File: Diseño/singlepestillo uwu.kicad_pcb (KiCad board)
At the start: 2 copper layers, 17 parts, among them J1 MAX98357A, J2 Conn_01x03_Pin, J3 Screw_Terminal_01x03, J5 Screw_Terminal_01x02, J9 Screw_Terminal_01x03, K3 G6AU, Q6 MMBT2222A, U3 EL817, U5 L7805, U6 ESP32DevKitv1

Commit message: avance pcb
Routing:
- net RV-VCC: track 151.4 -> 150.8 mm
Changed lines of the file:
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@@
-	)
-	(segment
-		(start 161.2 52.8)
-		(end 158.8 52.8)
-		(width 1)
-		(layer "B.Cu")
-		(net 3)
-	)
-	(segment
-		(start 158.8 52.8)
-		(end 153.4 47.4)
-		(width 1)
-		(layer "B.Cu")
-		(net 3)
 	)
 	(segment
@@
 	)
 	(segment
+		(start 161.758131 55.749)
+		(end 161.058131 55.049)
+		(width 1)
+		(layer "B.Cu")
+		(net 3)
+	)
+	(segment
 		(start 141.4 47.8)
 		(end 140.4 48.8)
@@
 	)
 	(segment
-		(start 163.891869 55.049)
-		(end 163.449 55.049)
+		(start 151.126 45.799)
+		(end 150.399 45.799)
 		(width 1)
 		(layer "B.Cu")
@@
 	)
 	(segment
-		(start 151.126 45.799)
-		(end 150.399 45.799)
+		(start 153.4 47.4)
+		(end 152.065 47.4)
+		(width 1)
+		(layer "B.Cu")
+		(net 3)
+	)
+	(segment
+		(start 163.449 55.749)
+		(end 161.758131 55.749)
+		(width 1)
+		(layer "B.Cu")
+		(net 3)
+	)
+	(segment
+		(start 161.049 55.049)
+		(end 153.4 47.4)
 		(width 1)
 		(layer "B.Cu")
@@
 	)
 	(segment
-		(start 165.7 58)
-		(end 163.891869 56.191869)
+		(start 133.069706 35.2)
+		(end 135.334853 37.465147)
 		(width 1)
 		(layer "B.Cu")
@@
 	)
 	(segment
-		(start 133.069706 35.2)
-		(end 135.334853 37.465147)
+		(start 161.058131 55.049)
+		(end 161.049 55.049)
 		(width 1)
 		(layer "B.Cu")
@@
 	)
 	(segment
-		(start 163.891869 56.191869)
-		(end 163.891869 55.049)
+		(start 165.7 58)
+		(end 163.449 55.749)
 		(width 1)
 		(layer "B.Cu")
@@
 		(width 1)
 		(layer "B.Cu")
-		(net 3)
-	)
-	(segment
-		(start 163.449 55.049)
-		(end 161.2 52.8)
-		(width 1)
-		(layer "B.Cu")
-		(net 3)
-	)
-	(segment
-		(start 153.4 47.4)
-		(end 152.065 47.4)
-		(width 1)
-		(layer "B.Cu")

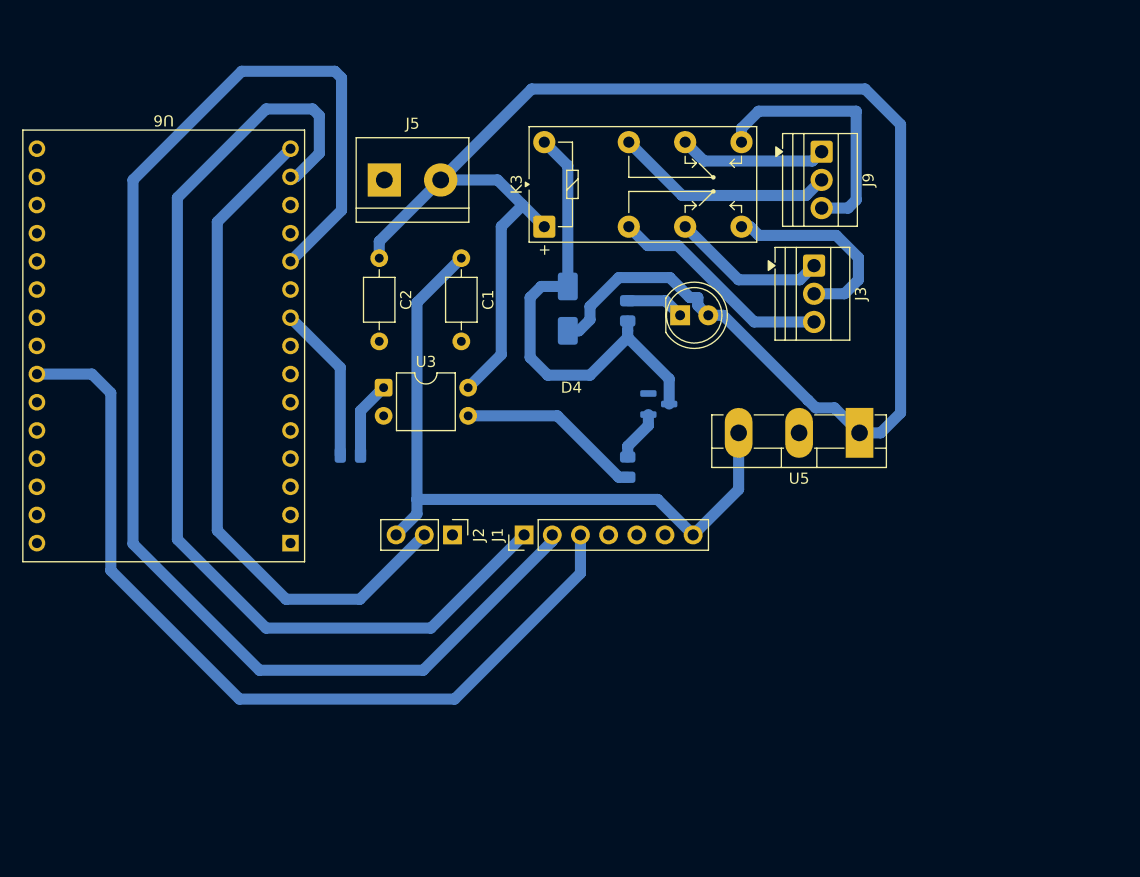
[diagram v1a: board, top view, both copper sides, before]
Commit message: correcion pcb y avance codigo
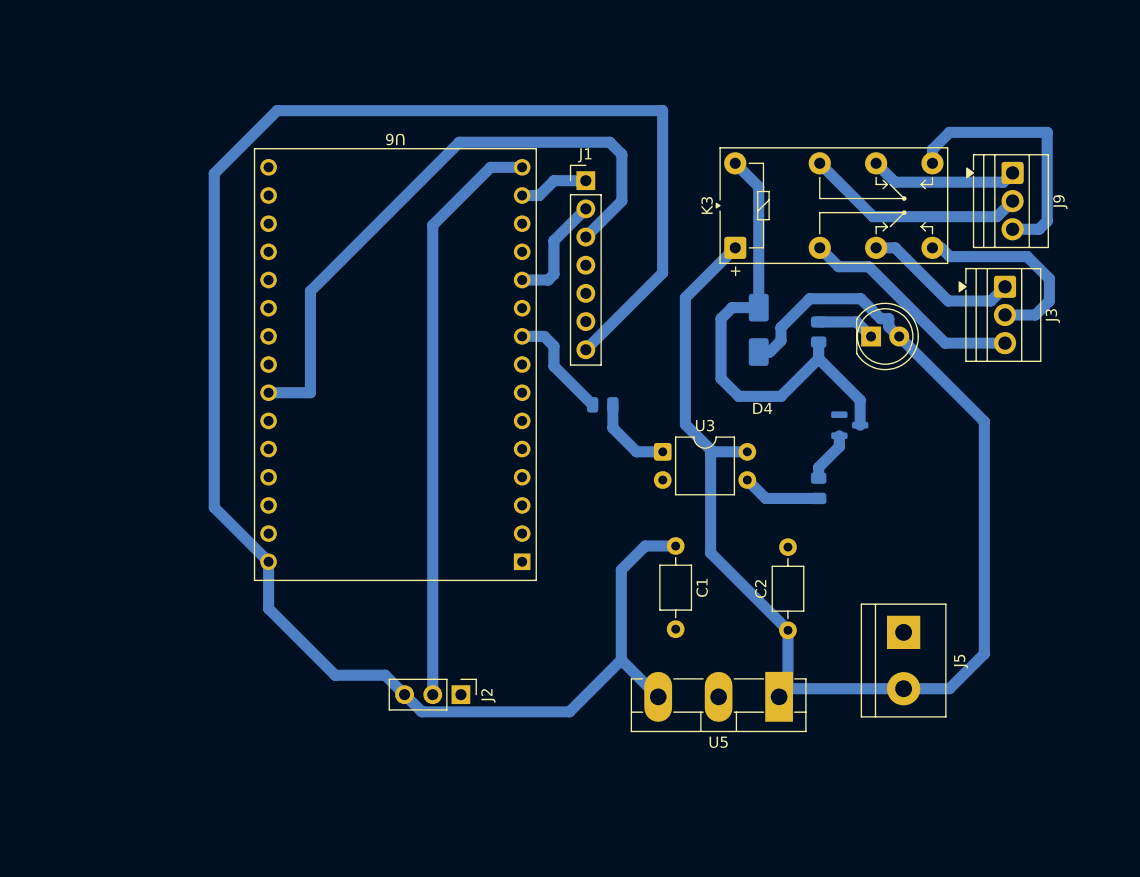
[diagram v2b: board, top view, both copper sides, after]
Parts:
- moved J5 62.1 mm to (169.7, 76.0), turned to -90 degrees
- moved C2 49.8 mm to (159.2, 75.8), turned to 90 degrees
- moved J1 32.4 mm to (141.0, 35.3), turned to 0 degrees
- moved C1 32.4 mm to (149.1, 68.2)
- moved U3 25.8 mm to (148.0, 59.7)
- moved U5 24.9 mm to (158.4, 81.8)
- moved R1 23.2 mm to (142.6, 55.5)
- moved U6 21.0 mm to (135.3, 69.6)
- moved D3 17.3 mm to (156.6, 48.7)
- moved D4 17.3 mm to (166.7, 49.3)
- moved J3 17.3 mm to (178.8, 44.8)
- moved J9 17.3 mm to (179.5, 34.6)
- moved K3 17.3 mm to (154.5, 41.3)
- moved Q6 17.3 mm to (164.8, 57.3)
- moved R2 17.3 mm to (162.0, 63.0)
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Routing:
- net GPIO21: track 122.3 -> 10.2 mm
- net +5V: track 64.5 -> 164.7 mm
- net GPIO22: track 92.1 -> 6.29 mm
- net RV-VCC: track 150.8 -> 118.9 mm
- net GPIO26: track 78.7 -> 55.8 mm
- net Net-(R2-Pad1): track 16.7 -> 7.12 mm
- net GPIO23: track 60.8 -> 52.5 mm
- net GPIO18: track 14.2 -> 9.97 mm
- net Net-(R1-Pad1): track 6.94 -> 7.47 mm

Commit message: Primer modelo final pcb
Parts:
- moved J2 51.8 mm to (125.5, 30.0)
- moved J1 34.1 mm to (107.0, 33.9)
- moved J5 23.0 mm to (151.5, 90.0), turned to 0 degrees
- moved D3 12.6 mm to (150.0, 38.0), turned to -90 degrees
- moved C2 7.80 mm to (159.0, 68.0), turned to -90 degrees
- moved Q6 4.35 mm to (162.0, 54.0), turned to 90 degrees
- moved R2 4.12 mm to (161.0, 59.0), turned to -90 degrees
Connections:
- J1 pad 3: GPIO26 -> GPIO19
- U6 pad 24: GPIO26 -> unconnected-(U6-D26-Pad24)
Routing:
- net GPIO19: track 0.00 -> 76.3 mm
- net GPIO26: track 55.8 -> 0.00 mm
- net GPIO21: track 10.2 -> 62.3 mm
- net RV-VCC: track 118.9 -> 167.1 mm
- net +5V: track 164.7 -> 122.7 mm
- net GPIO23: track 52.5 -> 15.6 mm
- net GPIO22: track 6.29 -> 42.6 mm
- net Net-(D3-A): track 43.0 -> 31.2 mm
- net Net-(R2-Pad1): track 7.12 -> 15.0 mm
- net Net-(Q6-B): track 4.60 -> 6.19 mm
- net GPIO18: track 9.97 -> 10.6 mm
- added copper zone on B.Cu, net GND
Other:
- board outline added: 90 x 75 mm

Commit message: Cambios en el amplificador del pcb, programacion actualizada
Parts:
- J1: value MAX98357A -> Conn_01x03_Pin; footprint Connector_PinHeader_2.54mm:PinHeader_1x07_P2.54mm_Vertical -> Connector_PinHeader_2.54mm:PinHeader_1x03_P2.54mm_Vertical
- moved J1 35.0 mm to (105.2, 68.8), turned to 180 degrees
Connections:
- J1 pad 1: GPIO22 -> GND
- J1 pad 2: GPIO21 -> +5V
- J1 pad 3: GPIO19 -> GPIO26
- U6 pad 10: GPIO19 -> unconnected-(U6-D19-Pad10)
- U6 pad 11: GPIO21 -> unconnected-(U6-D21-Pad11)
- U6 pad 24: unconnected-(U6-D26-Pad24) -> GPIO26
- U6 pad 6: GPIO16 -> unconnected-(U6-RX2/D16-Pad6)
- U6 pad 7: GPIO17 -> unconnected-(U6-TX2/D17-Pad7)
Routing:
- net GPIO19: track 76.3 -> 0.00 mm
- net GPIO21: track 62.3 -> 0.00 mm
- net GPIO22: track 42.6 -> 0.00 mm
- net +5V: track 122.7 -> 108.7 mm
- net GPIO26: track 0.00 -> 13.5 mm
- net GPIO23: track 15.6 -> 18.1 mm
- net RV-VCC: track 167.1 -> 168.6 mm

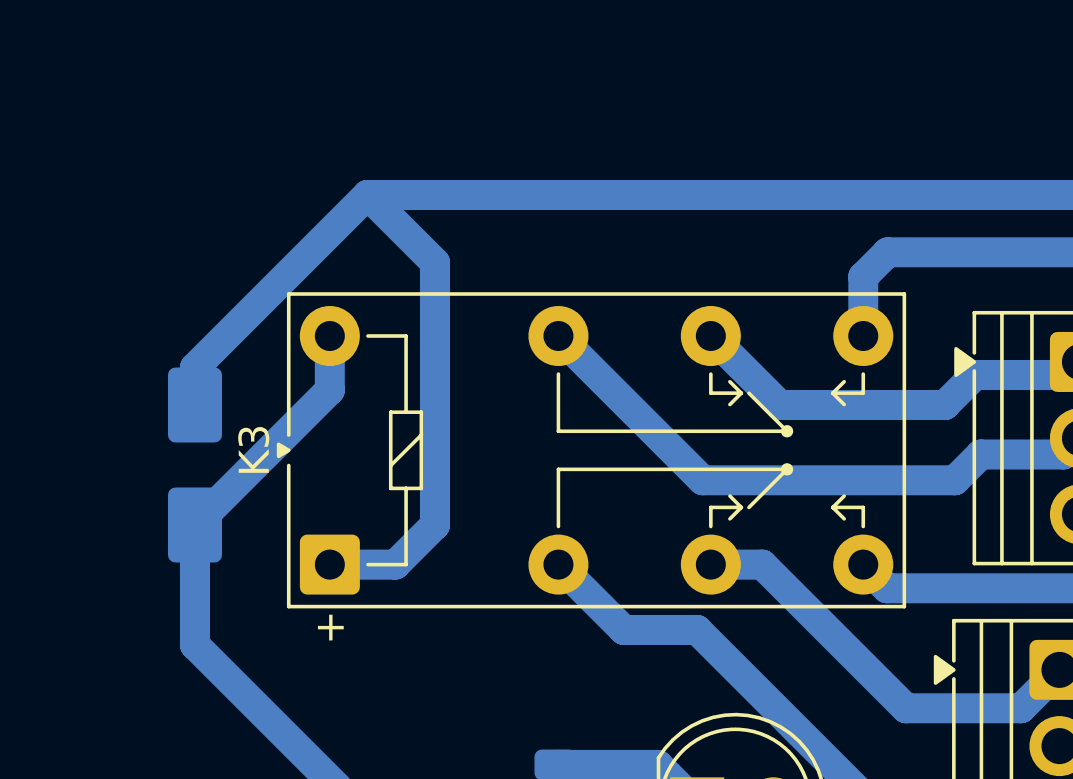
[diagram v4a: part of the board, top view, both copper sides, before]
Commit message: Optimizacion diseño del pcb
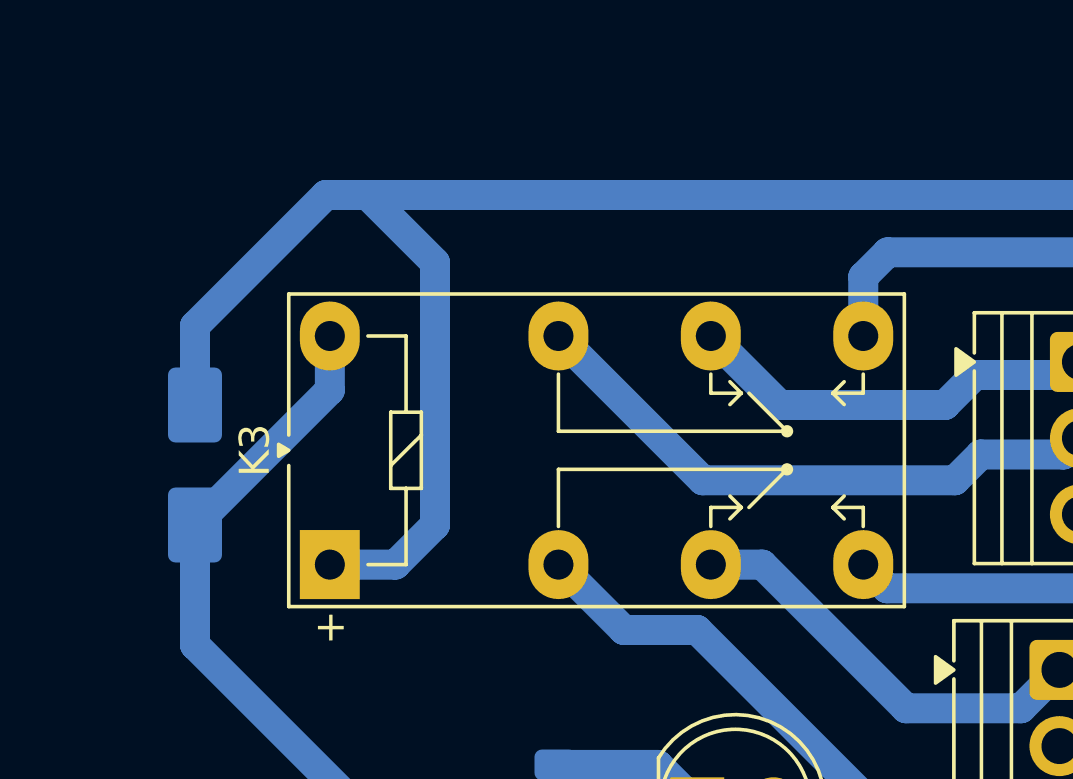
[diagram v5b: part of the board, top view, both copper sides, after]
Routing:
- net RV-VCC: track 168.6 -> 169.4 mm
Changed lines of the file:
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@@
 			)
 		)
-		(pad "11" thru_hole circle
+		(pad "11" thru_hole oval
 			(at 0 7.62 90)
-			(size 2 2)
+			(size 2.3 2)
 			(drill 1)
 			(layers "*.Cu" "*.Mask")
@@
 			(pintype "passive")
 		)
-		(pad "12" thru_hole circle
+		(pad "12" thru_hole oval
 			(at 0 12.7 90)
-			(size 2 2)
+			(size 2.3 2)
 			(drill 1)
 			(layers "*.Cu" "*.Mask")
@@
 			(pintype "passive")
 		)
-		(pad "14" thru_hole circle
+		(pad "14" thru_hole oval
 			(at 0 17.78 90)
-			(size 2 2)
+			(size 2.3 2)
 			(drill 1)
 			(layers "*.Cu" "*.Mask")
@@
 			(pintype "passive")
 		)
-		(pad "21" thru_hole circle
+		(pad "21" thru_hole oval
 			(at 7.62 7.62 90)
-			(size 2 2)
+			(size 2.3 2)
 			(drill 1)
 			(layers "*.Cu" "*.Mask")
@@
 			(pintype "passive")
 		)
-		(pad "22" thru_hole circle
+		(pad "22" thru_hole oval
 			(at 7.62 12.7 90)
-			(size 2 2)
+			(size 2.3 2)
 			(drill 1)
 			(layers "*.Cu" "*.Mask")
@@
 			(pintype "passive")
 		)
-		(pad "24" thru_hole circle
+		(pad "24" thru_hole oval
 			(at 7.62 17.78 90)
-			(size 2 2)
+			(size 2.3 2)
 			(drill 1)
 			(layers "*.Cu" "*.Mask")
@@
 			(pintype "passive")
 		)
-		(pad "A1" thru_hole roundrect
+		(pad "A1" thru_hole rect
 			(at 0 0 90)
-			(size 2 2)
+			(size 2.3 2)
 			(drill 1)
 			(layers "*.Cu" "*.Mask")
 			(remove_unused_layers no)
-			(roundrect_rratio 0.125)
 			(net 3 "RV-VCC")
 			(pintype "passive")
 		)
-		(pad "A2" thru_hole circle
+		(pad "A2" thru_hole oval
 			(at 7.62 0 90)
-			(size 2 2)
+			(size 2.3 2)
 			(drill 1)
 			(layers "*.Cu" "*.Mask")
@@
 	)
 	(segment
-		(start 150 36)
-		(end 150 34.75)
-		(width 1)
-		(layer "B.Cu")
-		(net 3)
-	)
-	(segment
 		(start 161.2 81.8)
 		(end 158.45 81.8)
@@
 	)
 	(segment
-		(start 150 34.75)
-		(end 155.75 29)
-		(width 1)
-		(layer "B.Cu")
-		(net 3)
-	)
-	(segment
 		(start 163 80)
 		(end 161.2 81.8)
@@
 	)
 	(segment
+		(start 154.36 29)
+		(end 155.75 29)
+		(width 1)
+		(layer "B.Cu")
+		(net 3)
+	)
+	(segment
+		(start 150 36)
+		(end 150 33.36)
+		(width 1)
+		(layer "B.Cu")
+		(net 3)
+	)
+	(segment
 		(start 185 29)
 		(end 155.75 29)
@@
 		(width 1)
 		(layer "B.Cu")
+		(net 3)
+	)
+	(segment
+		(start 150 33.36)
+		(end 154.36 29)
+		(width 1)
+		(layer "B.Cu")
